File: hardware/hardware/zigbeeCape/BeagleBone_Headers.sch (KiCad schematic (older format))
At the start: 2 parts, among them U4 BeagleBone_P8, U5 BeagleBone_P9

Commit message: Switchboardrev1 Complete
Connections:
- net UART_RX: now also U5.11 (UART4_RXD); no longer U5.26 (UART1_RXD)
- net UART_TX: now also U5.13 (UART4_TXD); no longer U5.24 (UART1_TXD)
- net FCON_RTS: now reaches U4.33 (LCD_DATA13)
- net BeagleBone_Reset: no longer names the net of U5.10 (SYS_RESETn)
- net LAN_Heartbeat: no longer names the net of U5.41 (GPIO_20)
- net Network_Connect: no longer names the net of U5.30 (GPIO_112)
- no-connect marks 71 -> 68
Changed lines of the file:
@@
 	1    0    0    -1
 $EndComp
-Text HLabel 5650 2250 0    50   Input ~ 0
-BeagleBone_Reset
-Text HLabel 7300 1550 2    50   Output ~ 0
-LAN_Heartbeat
-Text HLabel 7300 1950 2    50   Input ~ 0
-Network_Connect
-Text HLabel 5650 3650 0    50   Input ~ 0
+Text HLabel 5650 3850 0    50   Input ~ 0
 UART_TX
 Text HLabel 7250 3150 2    50   Input ~ 0
@@
 Text HLabel 7250 3850 2    50   BiDi ~ 0
 I2C2_SDA
-Text HLabel 5650 3750 0    50   Output ~ 0
+Text HLabel 5650 3950 0    50   Output ~ 0
 UART_RX
 $Comp
@@
 NoConn ~ 5800 3150
 NoConn ~ 5800 3050
-NoConn ~ 5800 3950
-NoConn ~ 5800 3850
 NoConn ~ 7100 3700
 NoConn ~ 7100 3600
@@
 NoConn ~ 2250 3550
 NoConn ~ 2250 3450
-NoConn ~ 2250 3350
 NoConn ~ 2250 3250
 NoConn ~ 2250 3150
@@
 Connection ~ 5650 1550
 Wire Wire Line
-	5800 2250 5650 2250
-Wire Wire Line
 	5800 2900 5650 2900
 Wire Wire Line
@@
 Connection ~ 5650 2500
 Wire Wire Line
-	5650 3650 5800 3650
-Wire Wire Line
-	5800 3750 5650 3750
-Wire Wire Line
 	7100 3950 7250 3950
 Wire Wire Line
@@
 	7250 3050 7100 3050
 Wire Wire Line
-	7100 1550 7300 1550
-Wire Wire Line
 	2250 1650 2050 1650
 Wire Wire Line
@@
 	2050 1550 2050 1650
 Connection ~ 2050 1650
+NoConn ~ 7100 1650
 Wire Wire Line
-	7100 1950 7300 1950
-NoConn ~ 7100 1650
+	5800 3950 5650 3950
+Wire Wire Line
+	5650 3850 5800 3850
+Text HLabel 2150 3350 0    50   Input ~ 0
+FCON_RTS
+Wire Wire Line
+	2250 3350 2150 3350
 $EndSCHEMATC

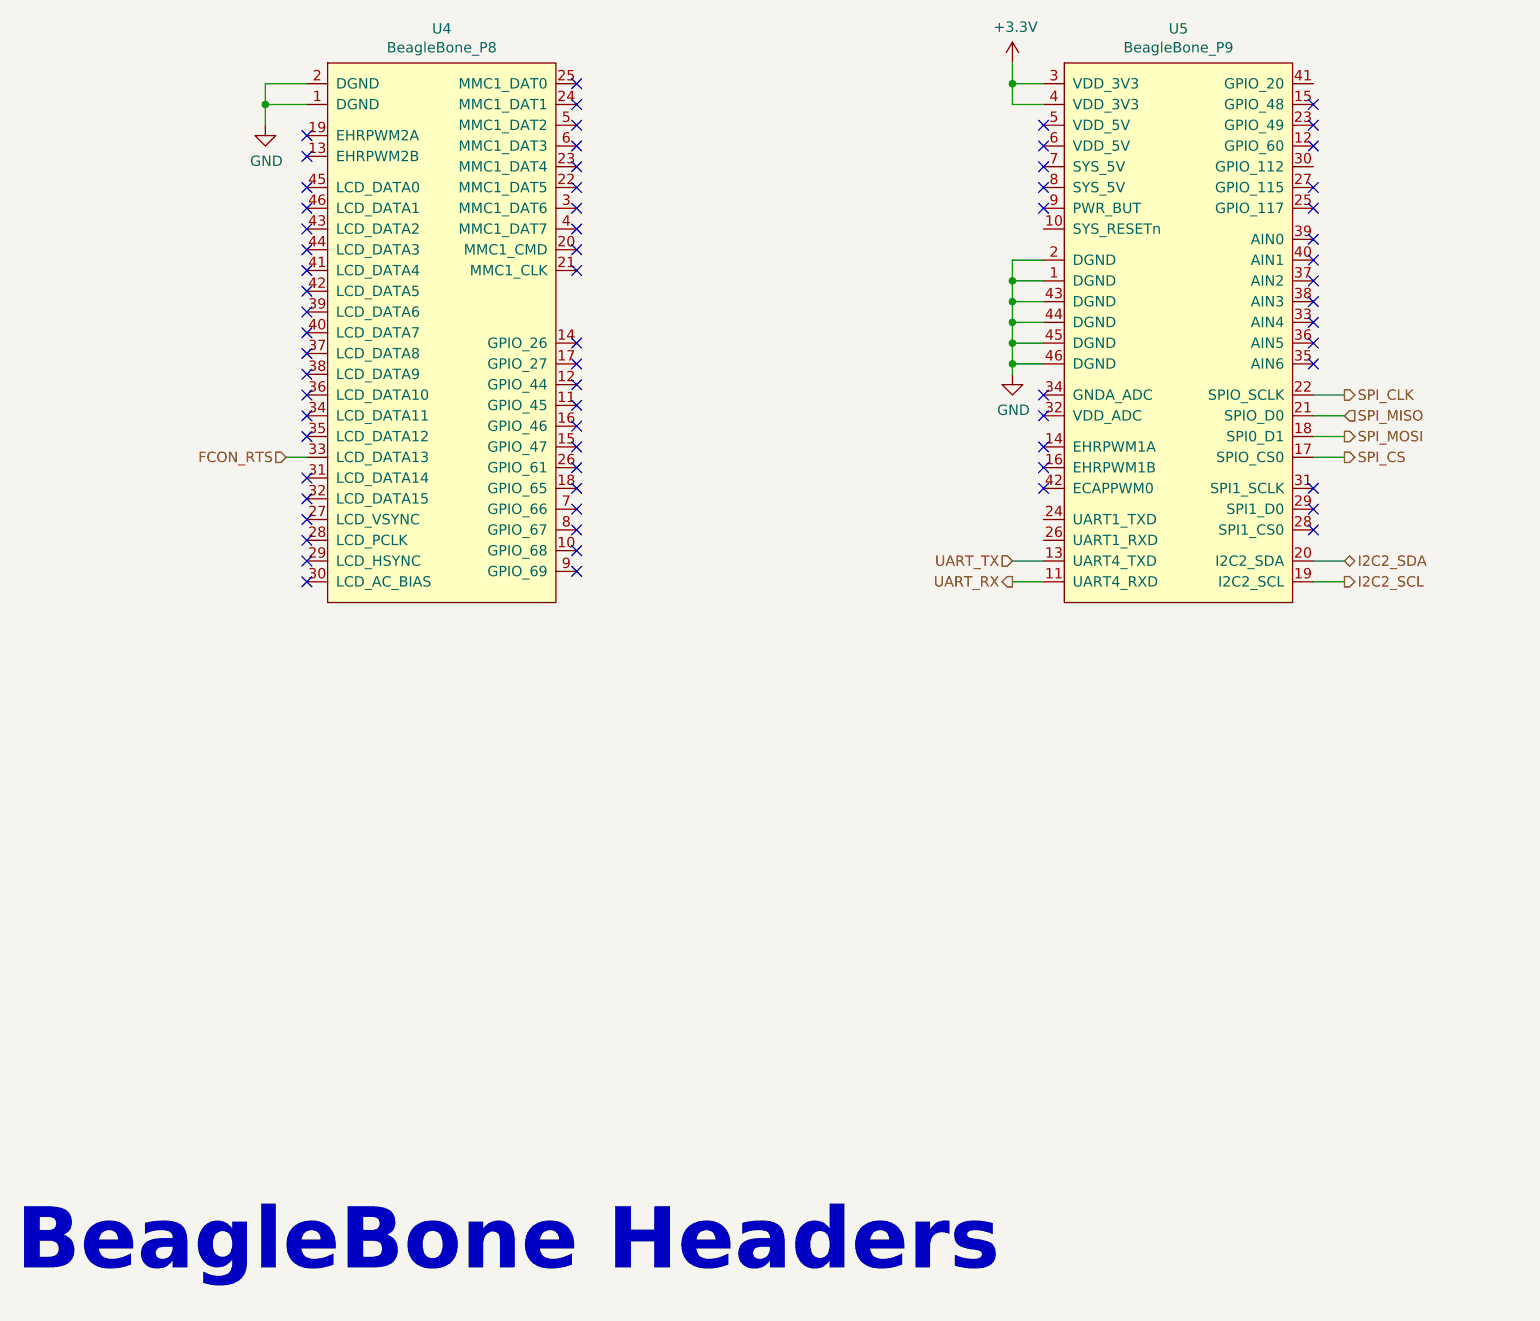
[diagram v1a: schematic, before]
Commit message: Cape_v2 schematic complete
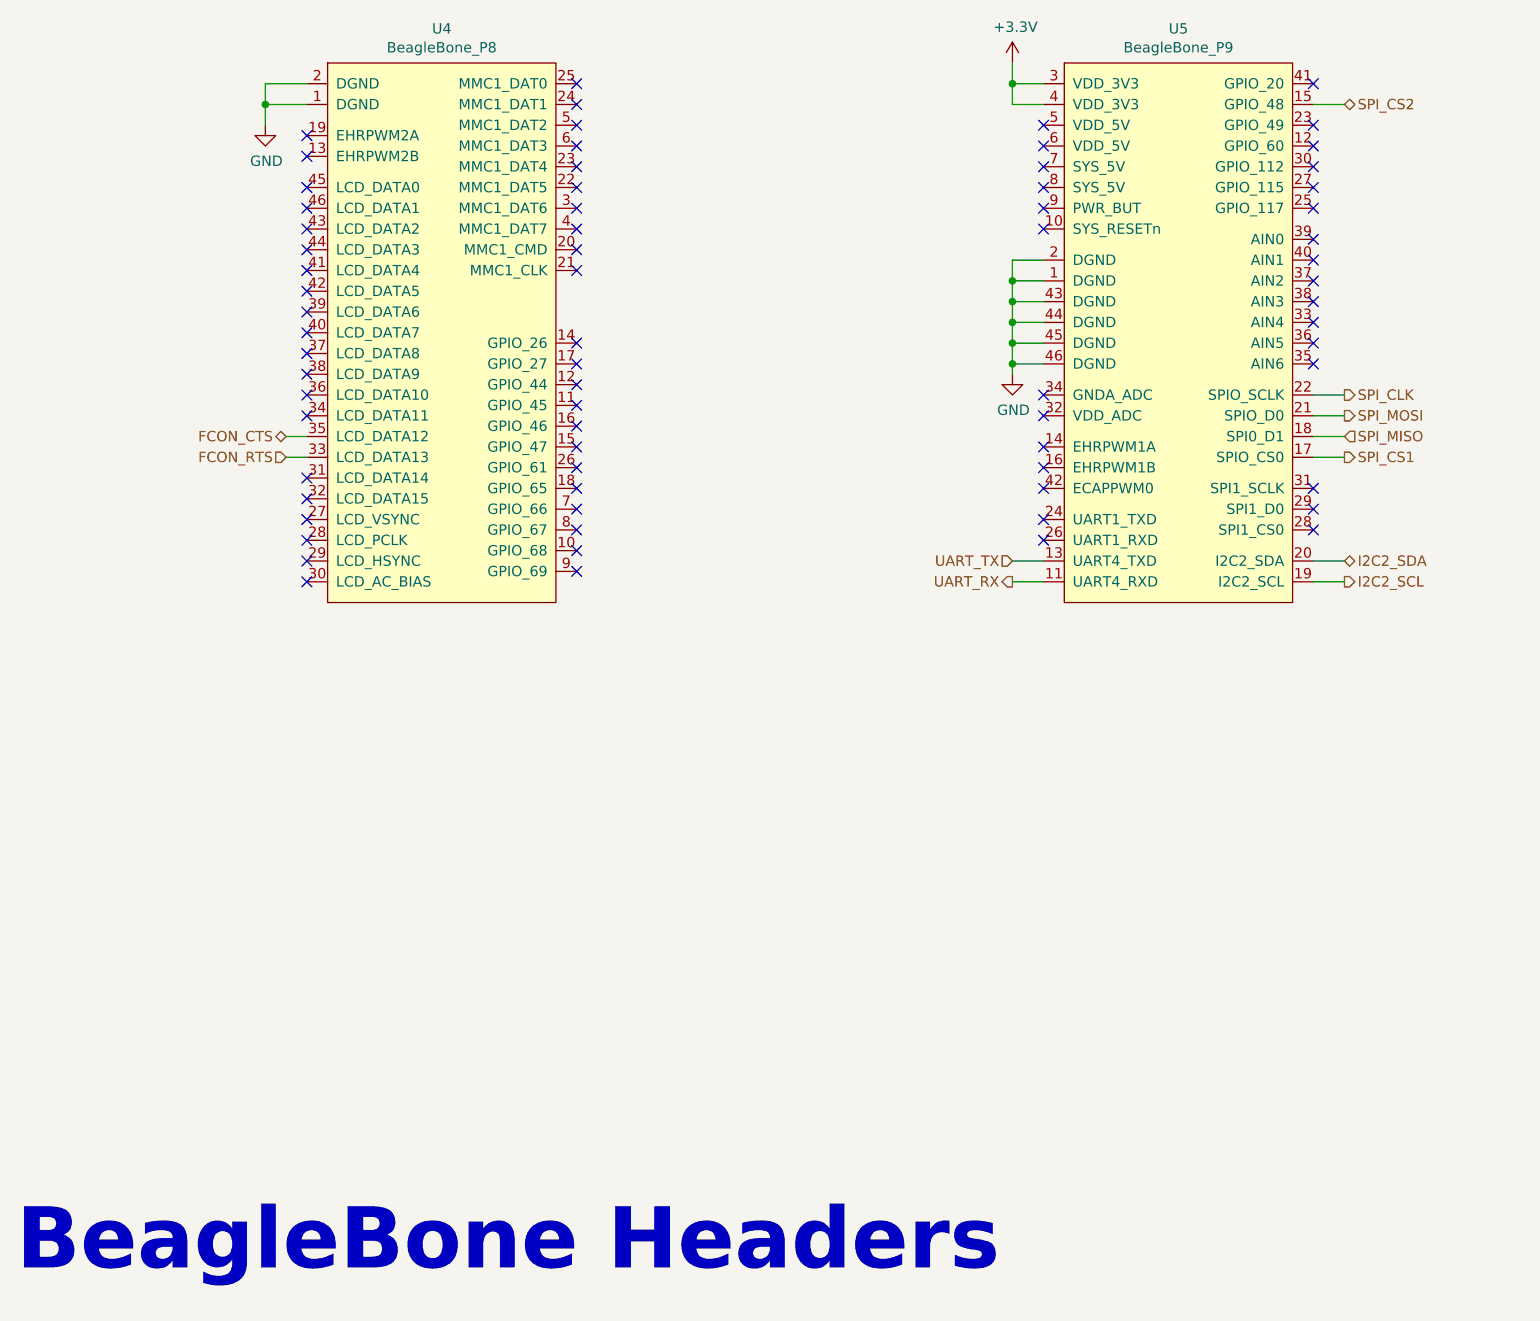
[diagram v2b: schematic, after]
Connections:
- net SPI_MISO: now also U5.18 (SPI0_D1); no longer U5.21 (SPIO_D0)
- net SPI_MOSI: now also U5.21 (SPIO_D0); no longer U5.18 (SPI0_D1)
- net FCON_CTS: now reaches U4.35 (LCD_DATA12)
- net SPI_CS2: now reaches U5.15 (GPIO_48)
- net SPI_CS renamed SPI_CS1
- no-connect marks 68 -> 71
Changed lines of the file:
@@
 Text HLabel 5650 3850 0    50   Input ~ 0
 UART_TX
-Text HLabel 7250 3150 2    50   Input ~ 0
+Text HLabel 7250 3250 2    50   Input ~ 0
 SPI_MISO
-Text HLabel 7250 3250 2    50   Output ~ 0
+Text HLabel 7250 3150 2    50   Output ~ 0
 SPI_MOSI
 Text HLabel 7250 3350 2    50   Output ~ 0
-SPI_CS
+SPI_CS1
 Text HLabel 7250 3050 2    50   Output ~ 0
 SPI_CLK
@@
 NoConn ~ 2250 3550
 NoConn ~ 2250 3450
-NoConn ~ 2250 3250
 NoConn ~ 2250 3150
 NoConn ~ 2250 3050
@@
 	7250 3350 7100 3350
 Wire Wire Line
-	7250 3250 7100 3250
-Wire Wire Line
-	7250 3150 7100 3150
-Wire Wire Line
 	7250 3050 7100 3050
 Wire Wire Line
@@
 	2050 1550 2050 1650
 Connection ~ 2050 1650
-NoConn ~ 7100 1650
-Wire Wire Line
-	5800 3950 5650 3950
-Wire Wire Line
-	5650 3850 5800 3850
 Text HLabel 2150 3350 0    50   Input ~ 0
 FCON_RTS
 Wire Wire Line
 	2250 3350 2150 3350
+Wire Wire Line
+	5650 3950 5800 3950
+Wire Wire Line
+	5650 3850 5800 3850
+Text HLabel 2150 3250 0    50   BiDi ~ 0
+FCON_CTS
+Wire Wire Line
+	2250 3250 2150 3250
+Wire Wire Line
+	7100 3250 7250 3250
+Wire Wire Line
+	7250 3150 7100 3150
+Text HLabel 7250 1650 2    50   BiDi ~ 0
+SPI_CS2
+Wire Wire Line
+	7100 1650 7250 1650
+NoConn ~ 7100 1550
+NoConn ~ 5800 2250
+NoConn ~ 7100 1950
+NoConn ~ 5800 3650
+NoConn ~ 5800 3750
 $EndSCHEMATC
